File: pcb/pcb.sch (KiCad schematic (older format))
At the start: 20 parts, among them J1 VIN VBAT, J2 Conn_01x04, J3 AudioJack3, J4 Conn_01x04, J5 HX711, J6 Conn_01x04, J7 Conn_01x04, J8 Conn_01x08, SW1 SW_DPDT_x2, U1 LM386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

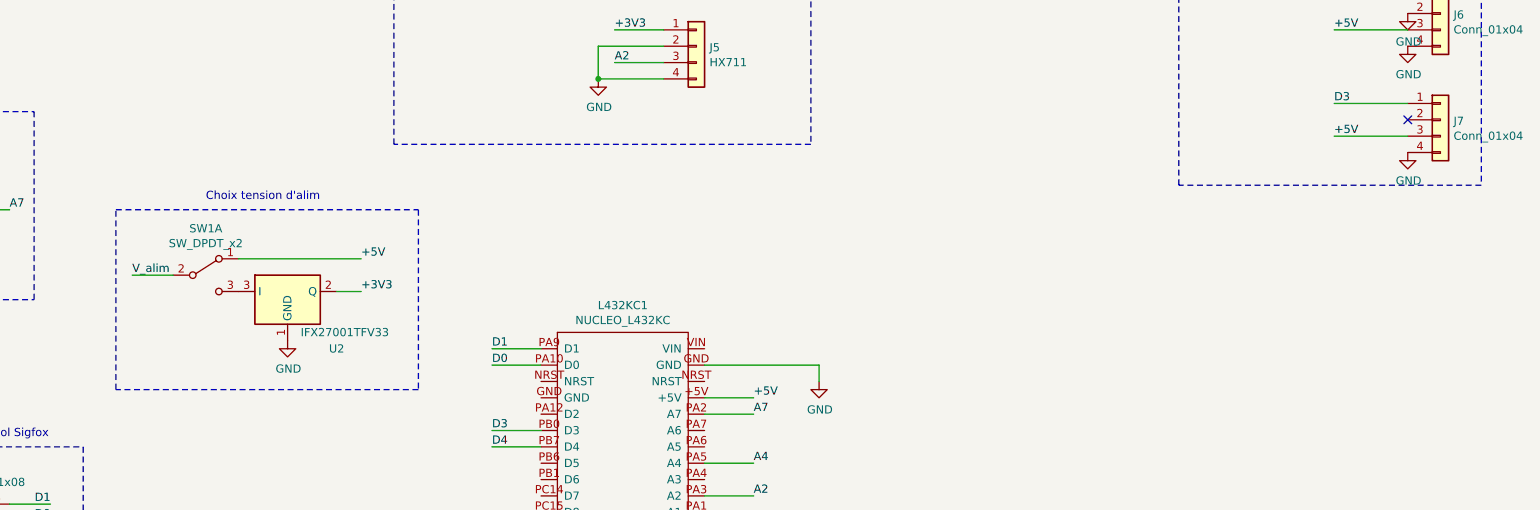
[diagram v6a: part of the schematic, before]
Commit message: Changement LDO et choix alim
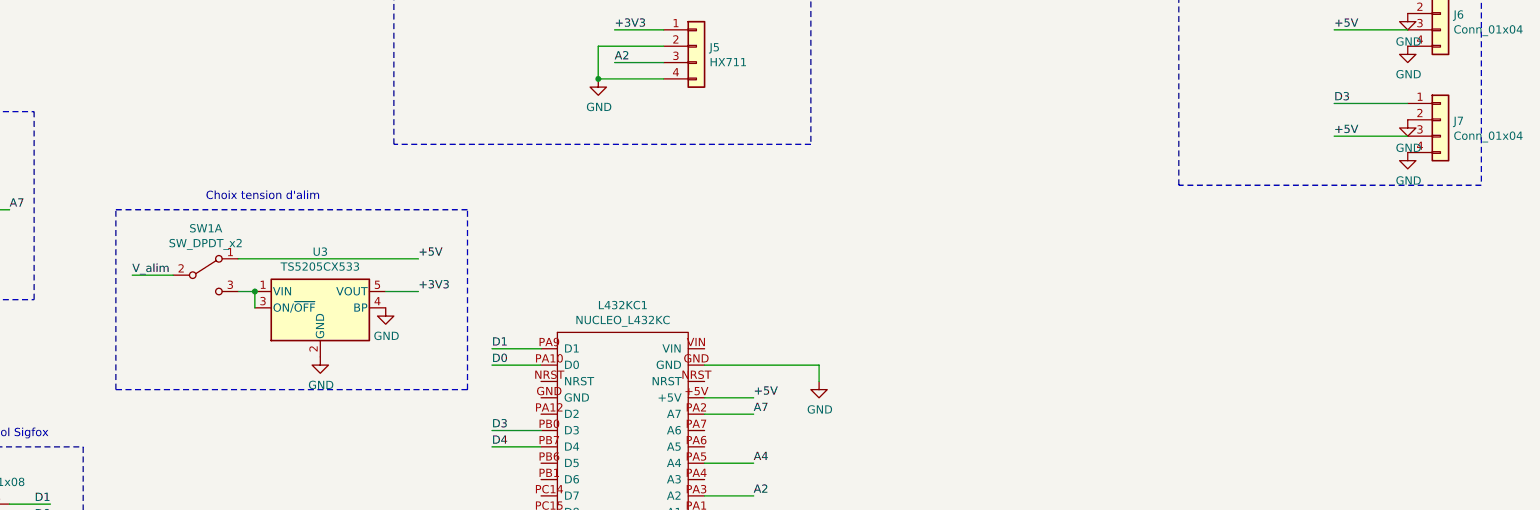
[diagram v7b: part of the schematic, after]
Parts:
- removed U2: IFX27001TFV33, Package_TO_SOT_SMD:TO-252-3_TabPin2, symbol Regulator_Linear:IFX27001TFV33
- added U3: TS5205CX533, Package_TO_SOT_SMD:SOT-23-5, symbol Regulator_Linear:LP2985-3.3
- SW1: footprint Button_Switch_SMD:SW_SPDT_CK-JS102011SAQN -> Connector_PinHeader_2.54mm:PinHeader_2x02_P2.54mm_Vertical
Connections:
- net +3V3: now also U3.5 (VOUT)
- net GND: now also J7.2 (Pin_2), U3.2 (GND), U3.4 (BP)
- net at SW1.3 (C): now also U3.1 (VIN), U3.3 (ON/~OFF~)
- no-connect marks 4 -> 3
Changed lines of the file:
@@
 Text Label 10200 1600 0    50   ~ 0
 D3
-NoConn ~ 10650 1700
 $Comp
 L Connector_Generic:Conn_01x04 J1
@@
 F 0 "SW1" H 3300 2935 50  0000 C CNN
 F 1 "SW_DPDT_x2" H 3300 2844 50  0000 C CNN
-F 2 "Button_Switch_SMD:SW_SPDT_CK-JS102011SAQN" H 3300 2650 50  0001 C CNN
+F 2 "Connector_PinHeader_2.54mm:PinHeader_2x02_P2.54mm_Vertical" H 3300 2650 50  0001 C CNN
 F 3 "~" H 3300 2650 50  0001 C CNN
 	1    3300 2650
@@
 Text Label 2850 2650 0    50   ~ 0
 V_alim
-$Comp
-L Regulator_Linear:IFX27001TFV33 U2
-U 1 1 5FBD8709
-P 3800 2750
-F 0 "U2" H 4100 2400 50  0000 C CNN
-F 1 "IFX27001TFV33" H 4150 2500 50  0000 C CNN
-F 2 "Package_TO_SOT_SMD:TO-252-3_TabPin2" H 3800 2700 50  0001 C CNN
-F 3 "https://static6.arrow.com/aropdfconversion/dc75757ae45a88e5f69bdce3f2a651a5fe0ca07d/ifx27001_ds_10.pdf" H 3800 2700 50  0001 C CNN
-	1    3800 2750
-	1    0    0    -1
-$EndComp
-$Comp
-L power:GND #PWR0120
-U 1 1 5FBD95A5
-P 3800 3050
-F 0 "#PWR0120" H 3800 2800 50  0001 C CNN
-F 1 "GND" H 3805 2877 50  0000 C CNN
-F 2 "" H 3800 3050 50  0001 C CNN
-F 3 "" H 3800 3050 50  0001 C CNN
-	1    3800 3050
-	1    0    0    -1
-$EndComp
-Wire Wire Line
-	3500 2550 4250 2550
-Wire Wire Line
-	4100 2750 4250 2750
-Text Label 4250 2550 0    50   ~ 0
-+5V
-Text Label 4250 2750 0    50   ~ 0
-+3V3
-Wire Notes Line
-	2750 2250 4600 2250
-Wire Notes Line
-	4600 2250 4600 3350
-Wire Notes Line
-	4600 3350 2750 3350
 Wire Notes Line
 	2750 3350 2750 2250
 Text Notes 3300 2200 0    50   ~ 0
 Choix tension d'alim
+$Comp
+L power:GND #PWR0121
+U 1 1 5FBF2942
+P 10650 1700
+F 0 "#PWR0121" H 10650 1450 50  0001 C CNN
+F 1 "GND" H 10655 1527 50  0000 C CNN
+F 2 "" H 10650 1700 50  0001 C CNN
+F 3 "" H 10650 1700 50  0001 C CNN
+	1    10650 1700
+	1    0    0    -1
+$EndComp
+$Comp
+L Regulator_Linear:LP2985-3.3 U3
+U 1 1 5FBD2C2A
+P 4000 2850
+F 0 "U3" H 4000 3192 50  0000 C CNN
+F 1 "TS5205CX533" H 4000 3101 50  0000 C CNN
+F 2 "Package_TO_SOT_SMD:SOT-23-5" H 4000 3175 50  0001 C CNN
+F 3 "http://www.ti.com/lit/ds/symlink/lp2985.pdf" H 4000 2850 50  0001 C CNN
+	1    4000 2850
+	1    0    0    -1
+$EndComp
+Wire Wire Line
+	4400 2750 4600 2750
+Wire Wire Line
+	3500 2550 4600 2550
+Wire Wire Line
+	3500 2750 3600 2750
+$Comp
+L power:GND #PWR0120
+U 1 1 5FBE4D4F
+P 4000 3150
+F 0 "#PWR0120" H 4000 2900 50  0001 C CNN
+F 1 "GND" H 4005 2977 50  0000 C CNN
+F 2 "" H 4000 3150 50  0001 C CNN
+F 3 "" H 4000 3150 50  0001 C CNN
+	1    4000 3150
+	1    0    0    -1
+$EndComp
+Wire Wire Line
+	3600 2850 3600 2750
+Connection ~ 3600 2750
+Text Label 4600 2550 0    50   ~ 0
++5V
+Text Label 4600 2750 0    50   ~ 0
++3V3
+Wire Notes Line
+	4900 3350 4900 2250
+Wire Notes Line
+	2750 2250 4900 2250
+Wire Notes Line
+	2750 3350 4900 3350
+$Comp
+L power:GND #PWR?
+U 1 1 5FBF27FC
+P 4400 2850
+F 0 "#PWR?" H 4400 2600 50  0001 C CNN
+F 1 "GND" H 4405 2677 50  0000 C CNN
+F 2 "" H 4400 2850 50  0001 C CNN
+F 3 "" H 4400 2850 50  0001 C CNN
+	1    4400 2850
+	1    0    0    -1
+$EndComp
 $EndSCHEMATC
